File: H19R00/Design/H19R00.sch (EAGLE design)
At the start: 115 parts, among them J1 691213710003, J2 691213710002, J3 20021121-00008T4LFU, J4 20021121-00006C1LF, U1 STM32G0B1CEU6N, U2 STSPIN32F0A, U3 AM26LV32EIRGYRTEXAS_INSTRUMEN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, U4 NCP730BMTADJTBGON_SEMI_NCP730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, X1 8MHZ

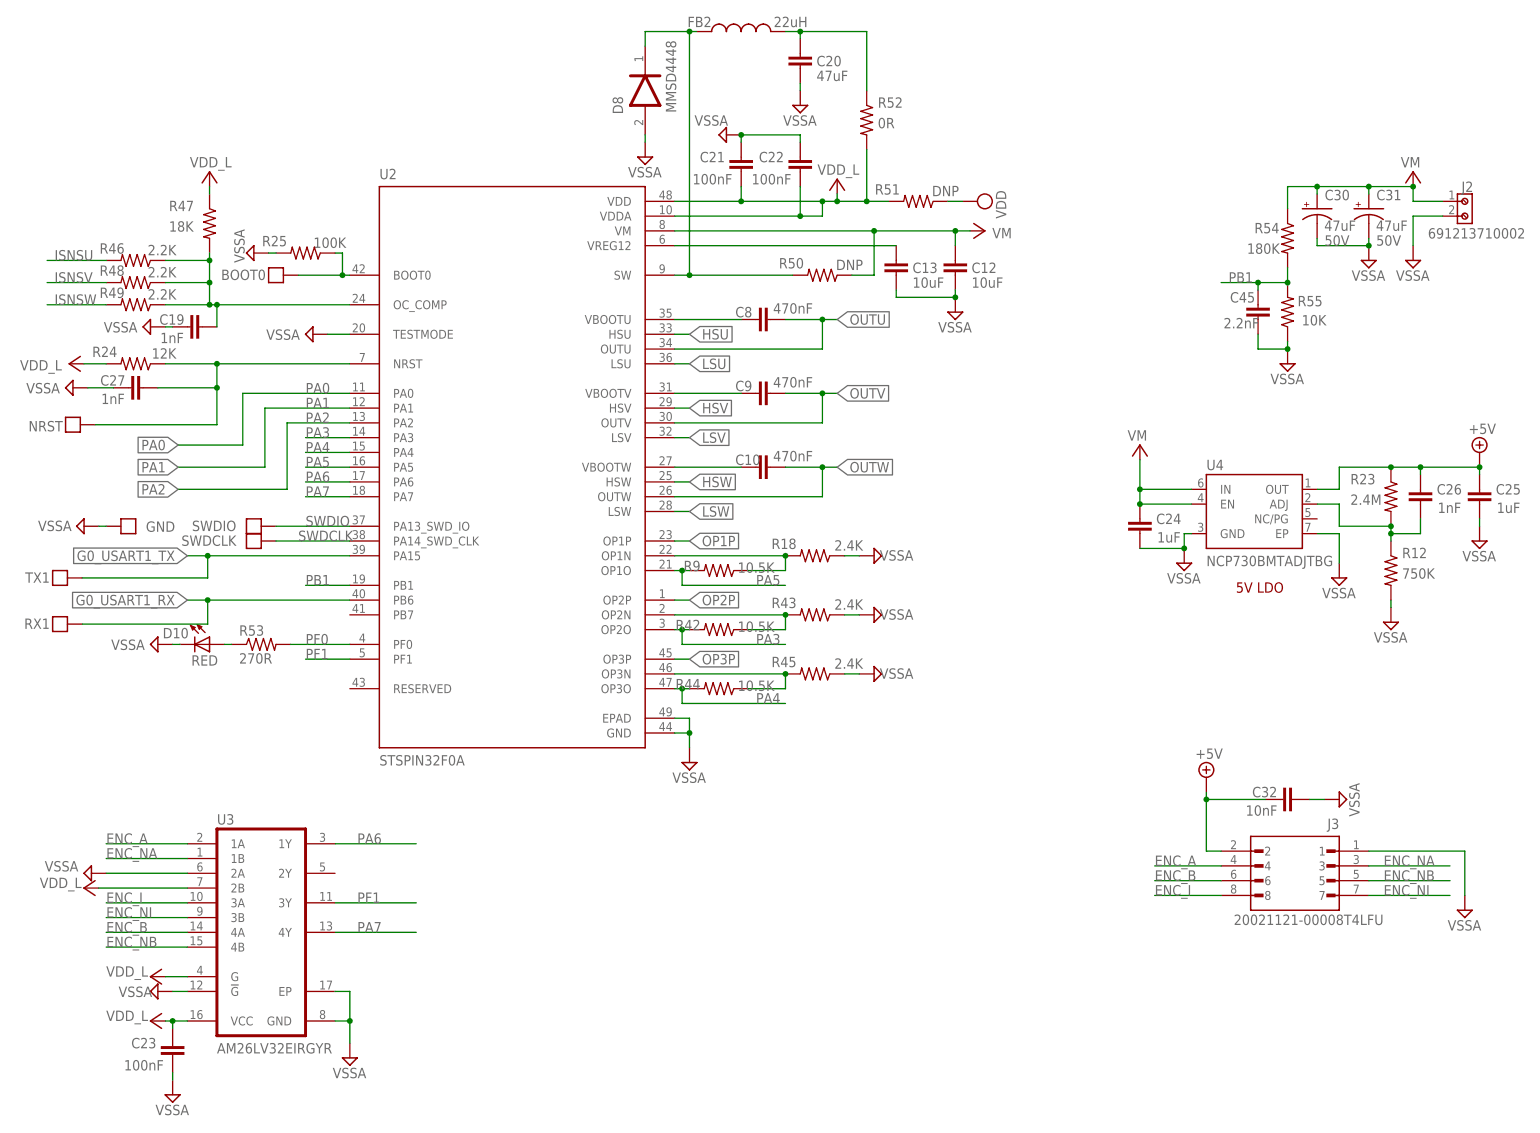
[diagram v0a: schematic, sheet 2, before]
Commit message: All the edits that is related to 10A handling is done : -Improve the layout design so the pcb can handle continous current up to 10A -Naming the smd pin headers and thier pins on the silk screen layer -Change the high voltage supply coupling smd capacitors to dip ones with bigger capacity - Edit the resistores values of the current sensing and comparator circuits to be compitable with the 10A and add the equtions as notes in the schematic
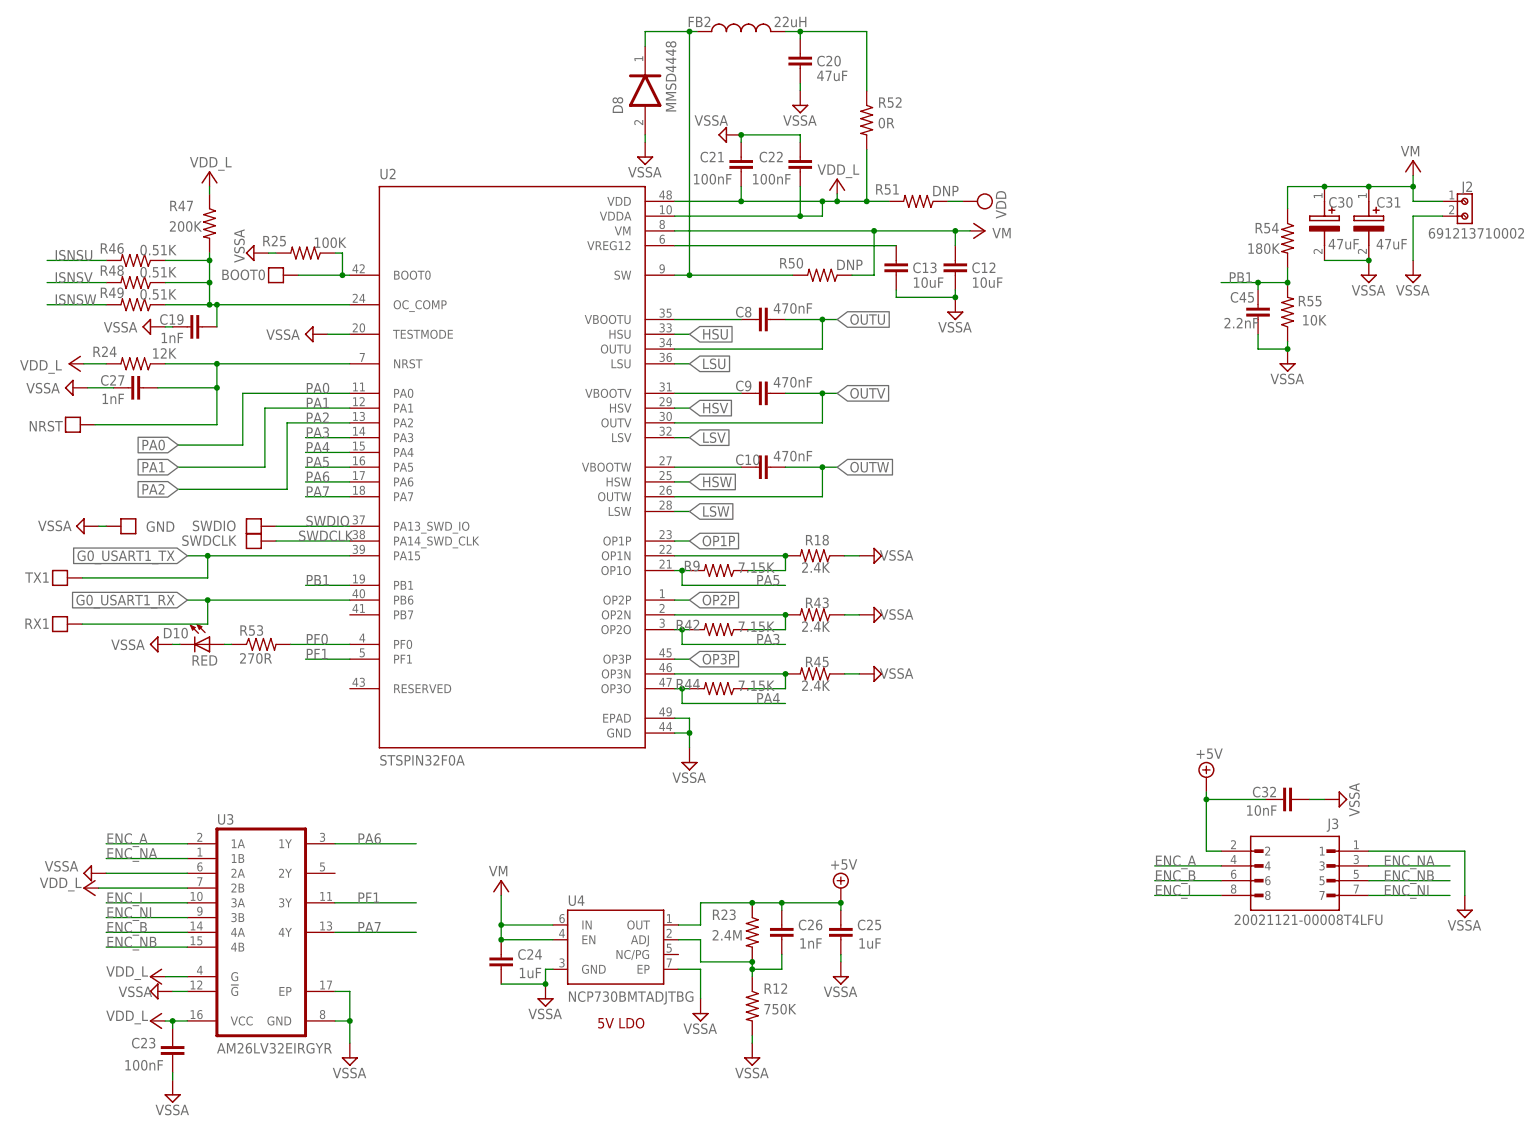
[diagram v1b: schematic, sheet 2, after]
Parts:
- C30, C31: device HEXABITZ_RCLS:A780EN476M1HLAS050 -> HEXABITZ_RCLS:UVR1H101MPD1TD
- R10, R14, R17: value 0.100R -> 0.050R
- R19, R21, R22, R41, R6, R7: value 21K -> 14.3K
- R42, R44, R9: value 10.5K -> 7.15K
- R46, R48, R49: value 2.2K -> 0.51K
- R47: value 18K -> 200K
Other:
- note added: "38 V/10A Sensored BLDC"
- note added: "H19R0"
- note added: "H19R0_Backened"
- note added: "H19R0_Frontened"
- note added: "OC_COMP Voltage = Vsense + Vp Vsense = (Isnsw+Isnsv+Isnsu)*Rsh * Rp / (Rn+3Rp) Vp = Vdd * Rn/(Rn+3Rp) ;Rp=R47 ; Rn = R46 = R48 = R49 ; Rsh=R10=R14=R17 Rsh = 0.05R , Rp = 200k ,Rn = 0.51k >>Isnsv+Isnsu+Isnsw > 29.85A .... OC_COMP = 500mV >>Isnsv+Isnsu+Isnsw > 14.84A .... OC_COMP = 250mV >>Isnsv+Isnsu+Isnsw > 5.83A ...... OC_COMP = 100mV"
- note added: "￼OPO=Gain*(Rp1*Isns(w,u,v)*Rsh + Rn1*3.3) Gain=1+Rf/Rn1 ;Rn1=R18=R43=R45=R40=R20=R8 ;Rp1=R22=R41=R19=R21=R7=R6 ;Rf=R9=R42=R44 ; Rsh=R10=R14=R17 ;Rsh=0.05R & Rf=7.15k & Rp1=14.3k & Rn1=2.4k >>Isns(w,u,v)[0-10]A >>OPO (1.65 - 3.14) V"
- note removed: "36 V/6A Sensored BLDC"
- note removed: "H19R00"
- note removed: "H19R00_Backened"
- note removed: "H19R00_Frontened"
- moved on the sheet: C24, C25, C26, J1, R12, R23, U4
